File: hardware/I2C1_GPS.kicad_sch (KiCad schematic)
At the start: 0 parts

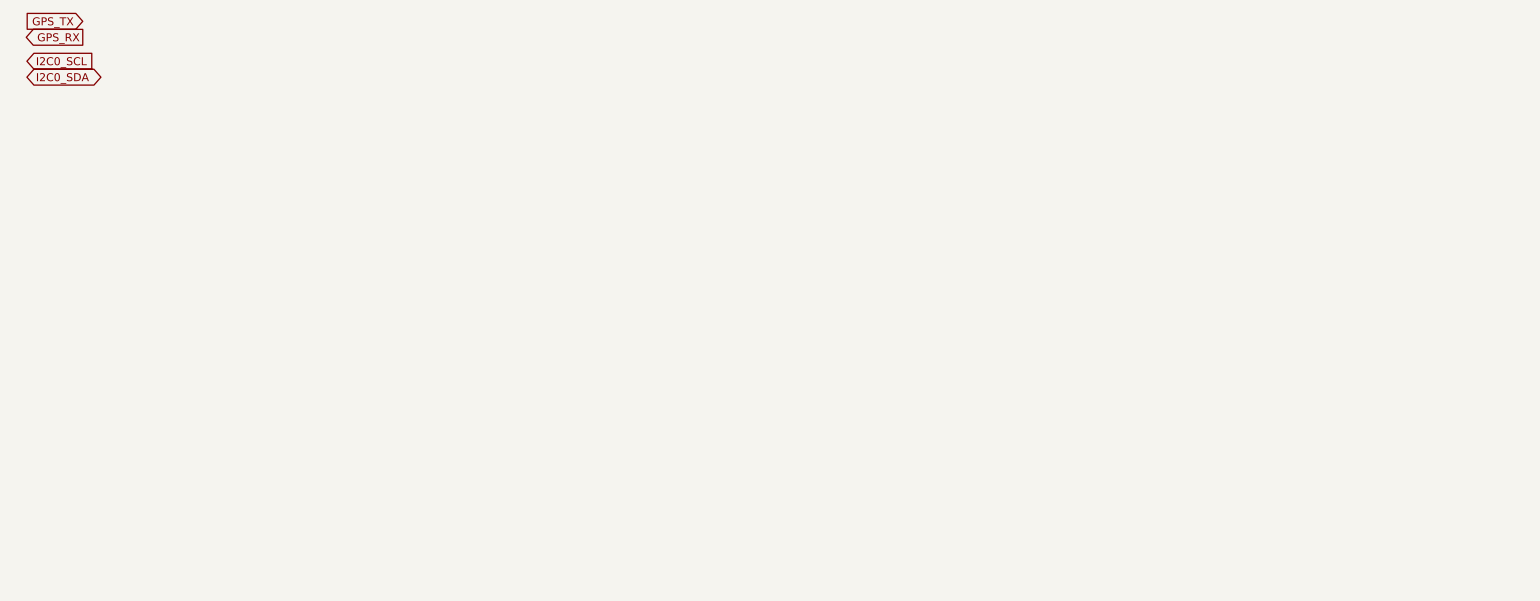
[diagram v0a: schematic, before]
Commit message: More work on the scehmatic for I2C0 and I2C1 + UART GPS.
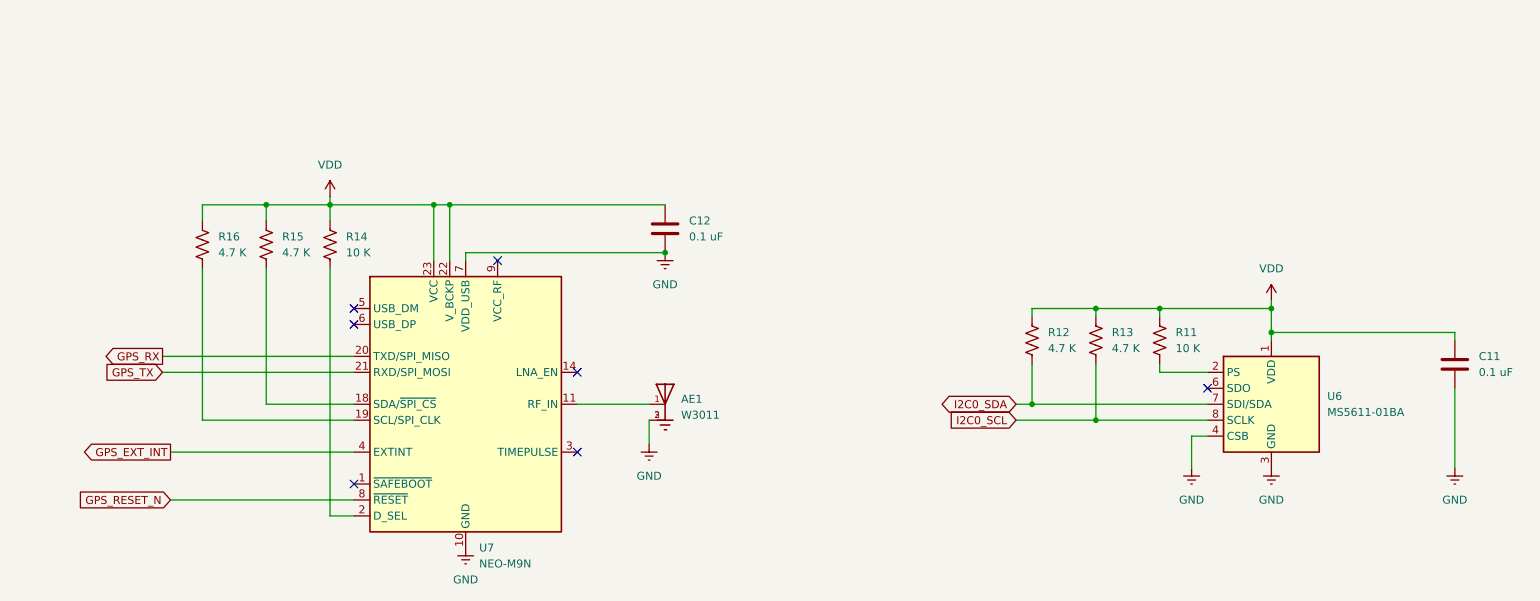
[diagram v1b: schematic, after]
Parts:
- added AE1: W3011, W3011:XDCR_W3011, symbol W3011:W3011
- added C11, C12: 0.1 uF, symbol Device:C
- added R11, R14: 10 K, symbol Device:R_US
- added R12, R13, R15, R16: 4.7 K, symbol Device:R_US
- added U6: MS5611-01BA, Package_LGA:LGA-8_3x5mm_P1.25mm, symbol Sensor_Pressure:MS5611-01BA
- added U7: NEO-M9N, RF_GPS:ublox_NEO, symbol RF_GPS:NEO-M9N
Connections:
- net GPS_RX: now also U7.20 (TXD/SPI_MISO)
- net GPS_TX: now also U7.21 (RXD/SPI_MOSI)
- net I2C0_SCL: now also R13.1, U6.8 (SCLK)
- net I2C0_SDA: now also R12.1, U6.7 (SDI/SDA)
- new net: R11.1, U6.2 (PS)
- new net: AE1.1, U7.11 (RF_IN)
- new net: R15.2, U7.18 (SDA/~{SPI_CS})
- new net: R16.2, U7.19 (SCL/SPI_CLK)
- new net: R14.2, U7.2 (D_SEL)
- new net GND: AE1.2, AE1.3, C11.2, C12.2, U6.3 (GND), U6.4 (CSB), U6.5 (CSB), U7.10 (GND), U7.12 (GND), U7.13 (GND), U7.24 (GND), U7.7 (VDD_USB)
- new net GPS_EXT_INT: U7.4 (EXTINT)
- new net GPS_RESET_N: U7.8 (~{RESET})
- new net VDD: C11.1, C12.1, R11.2, R12.2, R13.2, R14.1, R15.1, R16.1, U6.1 (VDD), U7.22 (V_BCKP), U7.23 (VCC)
- no-connect marks 0 -> 7

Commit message: Fixed EEC errors.
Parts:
- AE1: footprint W3011:XDCR_W3011 -> footprints:XDCR_W3011
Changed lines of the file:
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@@
 			)
 		)
-		(property "Footprint" "W3011:XDCR_W3011"
+		(property "Footprint" "footprints:XDCR_W3011"
 			(at 119.38 80.01 0)
 			(hide yes)

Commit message: Added footprints for the resitors.
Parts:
- R11, R12, R13, R14, R15, R16: footprint (none) -> Resistor_SMD:R_1206_3216Metric
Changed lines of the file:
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@@
 			)
 		)
-		(property "Footprint" ""
+		(property "Footprint" "Resistor_SMD:R_1206_3216Metric"
 			(at 197.104 69.596 90)
 			(hide yes)
@@
 			)
 		)
-		(property "Footprint" ""
+		(property "Footprint" "Resistor_SMD:R_1206_3216Metric"
 			(at 186.944 69.596 90)
 			(hide yes)
@@
 			)
 		)
-		(property "Footprint" ""
+		(property "Footprint" "Resistor_SMD:R_1206_3216Metric"
 			(at 67.056 54.864 90)
 			(hide yes)
@@
 			)
 		)
-		(property "Footprint" ""
+		(property "Footprint" "Resistor_SMD:R_1206_3216Metric"
 			(at 176.784 69.596 90)
 			(hide yes)
@@
 			)
 		)
-		(property "Footprint" ""
+		(property "Footprint" "Resistor_SMD:R_1206_3216Metric"
 			(at 56.896 54.864 90)
 			(hide yes)
@@
 			)
 		)
-		(property "Footprint" ""
+		(property "Footprint" "Resistor_SMD:R_1206_3216Metric"
 			(at 46.736 54.864 90)
 			(hide yes)

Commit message: Added capacitor footprints.
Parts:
- C11, C12: footprint (none) -> Capacitor_SMD:C_1206_3216Metric
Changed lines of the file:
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@@
 			)
 		)
-		(property "Footprint" ""
+		(property "Footprint" "Capacitor_SMD:C_1206_3216Metric"
 			(at 246.0752 77.47 0)
 			(hide yes)
@@
 			)
 		)
-		(property "Footprint" ""
+		(property "Footprint" "Capacitor_SMD:C_1206_3216Metric"
 			(at 120.3452 55.88 0)
 			(hide yes)

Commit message: Worked on footprints and hardware definations.
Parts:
- C11, C12: footprint Capacitor_SMD:C_1206_3216Metric -> Capacitor_SMD:C_0805_2012Metric; Digikey Link (none) -> https://www.digikey.com/en/products/detail/kyocera-avx/KGM2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; Digikey Part Number (none) -> 478-KGM21NR71H104KTCT-ND
- R11, R14: value 10 K -> 10k
- R12, R13, R15, R16: value 4.7 K -> 4.7k
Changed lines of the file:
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@@
 			)
 		)
-		(property "Value" "10 K"
+		(property "Value" "10k"
 			(at 200.66 71.1199 0)
 			(show_name no)
@@
 			)
 		)
-		(property "Value" "4.7 K"
+		(property "Value" "4.7k"
 			(at 190.5 71.1199 0)
 			(show_name no)
@@
 			)
 		)
-		(property "Value" "10 K"
+		(property "Value" "10k"
 			(at 68.58 55.8799 0)
 			(show_name no)
@@
 			)
 		)
-		(property "Value" "4.7 K"
+		(property "Value" "4.7k"
 			(at 180.34 71.1199 0)
 			(show_name no)
@@
 			)
 		)
-		(property "Value" "4.7 K"
+		(property "Value" "4.7k"
 			(at 58.42 55.8799 0)
 			(show_name no)
@@
 			)
 		)
-		(property "Footprint" "Capacitor_SMD:C_1206_3216Metric"
+		(property "Footprint" "Capacitor_SMD:C_0805_2012Metric"
 			(at 246.0752 77.47 0)
 			(hide yes)
@@
 			)
 		)
+		(property "Digikey Link" "https://www.digikey.com/en/products/detail/kyocera-avx/KGM21NR71H104KT/563505"
+			(at 245.11 73.66 0)
+			(hide yes)
+			(show_name no)
+			(do_not_autoplace no)
+			(effects
+				(font
+					(size 1.27 1.27)
+				)
+			)
+		)
+		(property "Digikey Part Number" "478-KGM21NR71H104KTCT-ND"
+			(at 245.11 73.66 0)
+			(hide yes)
+			(show_name no)
+			(do_not_autoplace no)
+			(effects
+				(font
+					(size 1.27 1.27)
+				)
+			)
+		)
 		(pin "1"
 		)
@@
 			)
 		)
-		(property "Footprint" "Capacitor_SMD:C_1206_3216Metric"
+		(property "Footprint" "Capacitor_SMD:C_0805_2012Metric"
 			(at 120.3452 55.88 0)
 			(hide yes)
@@
 			)
 		)
+		(property "Digikey Link" "https://www.digikey.com/en/products/detail/kyocera-avx/KGM21NR71H104KT/563505"
+			(at 119.38 52.07 0)
+			(hide yes)
+			(show_name no)
+			(do_not_autoplace no)
+			(effects
+				(font
+					(size 1.27 1.27)
+				)
+			)
+		)
+		(property "Digikey Part Number" "478-KGM21NR71H104KTCT-ND"
+			(at 119.38 52.07 0)
+			(hide yes)
+			(show_name no)
+			(do_not_autoplace no)
+			(effects
+				(font
+					(size 1.27 1.27)
+				)
+			)
+		)
 		(pin "1"
 		)
@@
 			)
 		)
-		(property "Value" "4.7 K"
+		(property "Value" "4.7k"
 			(at 48.26 55.8799 0)
 			(show_name no)

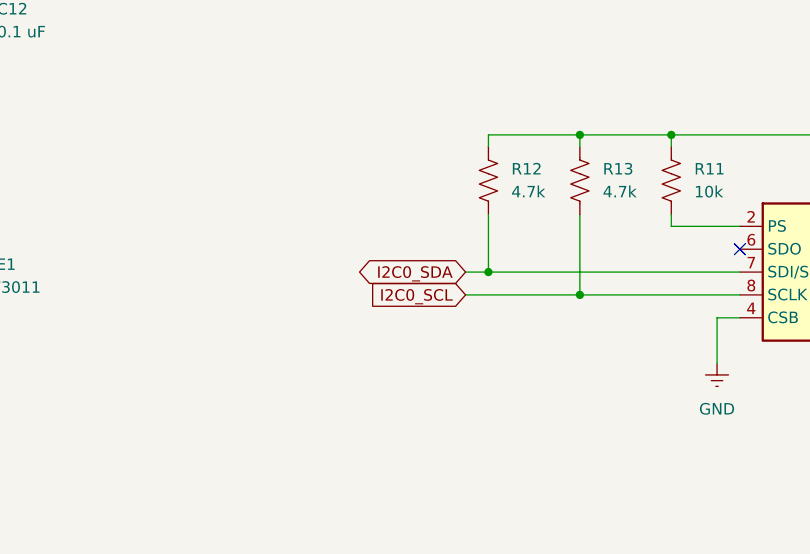
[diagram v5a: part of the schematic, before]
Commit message: Fixed I2C1 global labels.
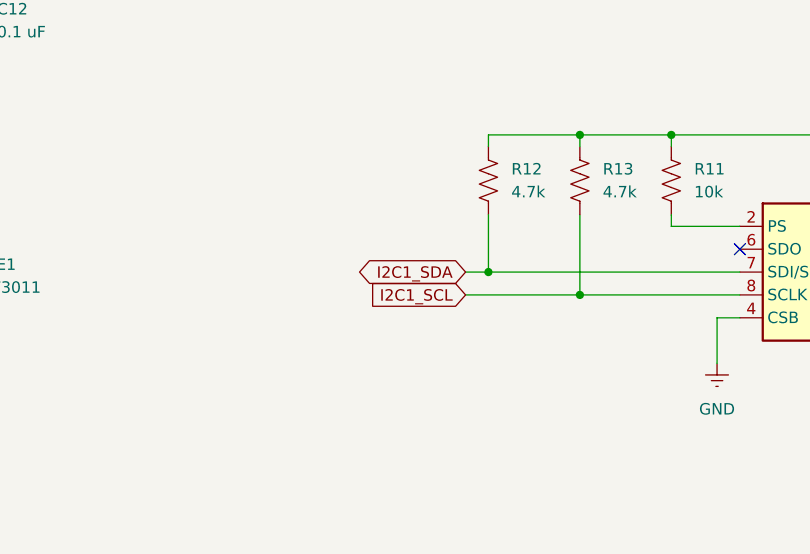
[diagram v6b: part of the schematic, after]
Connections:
- net I2C0_SCL renamed I2C1_SCL
- net I2C0_SDA renamed I2C1_SDA
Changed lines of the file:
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@@
 		)
 	)
-	(global_label "I2C0_SCL"
+	(global_label "I2C1_SCL"
 		(shape input)
 		(at 175.26 82.55 180)
@@
 		)
 	)
-	(global_label "I2C0_SDA"
+	(global_label "I2C1_SDA"
 		(shape bidirectional)
 		(at 175.26 80.01 180)

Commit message: Worked on PCB routing and component placement.
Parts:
- AE1: Digikey Link (none) -> https://www.digikey.com/en/products/detail/pulse-electronic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; Digikey Part Number (none) -> 553-2582-1-ND
- R11, R14: footprint Resistor_SMD:R_1206_3216Metric -> Resistor_SMD:R_0603_1608Metric; Digikey Link (none) -> https://www.digikey.com/en/products/detail/vishay/MCT06030C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; Digikey Part Number (none) -> MCT0603-10.0K-CFCT-ND
- R12, R13, R15, R16: footprint Resistor_SMD:R_1206_3216Metric -> Resistor_SMD:R_0603_1608Metric; Digikey Link (none) -> https://www.digikey.com/en/products/detail/vishay/MCT06030C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; Digikey Part Number (none) -> MCT0603-4.70K-CFCT-ND
- U6: Digikey Link (none) -> https://www.digikey.com/en/products/detail/te-connectivity-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; Digikey Part Number (none) -> 223-1622-1-ND
- U7: Digikey Link (none) -> https://www.digikey.com/en/products/detail/u-blox/NEO-M9N-0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; Digikey Part Number (none) -> 672-NEO-M9N-00BCT-ND
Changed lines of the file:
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@@
 			)
 		)
-		(property "Footprint" "Resistor_SMD:R_1206_3216Metric"
+		(property "Footprint" "Resistor_SMD:R_0603_1608Metric"
 			(at 197.104 69.596 90)
 			(hide yes)
@@
 		)
 		(property "Description" "Resistor, US symbol"
+			(at 198.12 69.85 0)
+			(hide yes)
+			(show_name no)
+			(do_not_autoplace no)
+			(effects
+				(font
+					(size 1.27 1.27)
+				)
+			)
+		)
+		(property "Digikey Link" "https://www.digikey.com/en/products/detail/vishay/MCT06030C1002FP500/1850440"
+			(at 198.12 69.85 0)
+			(hide yes)
+			(show_name no)
+			(do_not_autoplace no)
+			(effects
+				(font
+					(size 1.27 1.27)
+				)
+			)
+		)
+		(property "Digikey Part Number" "MCT0603-10.0K-CFCT-ND"
 			(at 198.12 69.85 0)
 			(hide yes)
@@
 			)
 		)
+		(property "Digikey Link" "https://www.digikey.com/en/products/detail/pulse-electronics/W3011/3025804"
+			(at 119.38 80.01 0)
+			(hide yes)
+			(show_name no)
+			(do_not_autoplace no)
+			(effects
+				(font
+					(size 1.27 1.27)
+				)
+			)
+		)
+		(property "Digikey Part Number" "553-2582-1-ND"
+			(at 119.38 80.01 0)
+			(hide yes)
+			(show_name no)
+			(do_not_autoplace no)
+			(effects
+				(font
+					(size 1.27 1.27)
+				)
+			)
+		)
 		(pin "3"
 		)
@@
 			)
 		)
+		(property "Digikey Link" "https://www.digikey.com/en/products/detail/te-connectivity-measurement-specialties/MS561101BA03-50/5277445"
+			(at 215.9 80.01 0)
+			(hide yes)
+			(show_name no)
+			(do_not_autoplace no)
+			(effects
+				(font
+					(size 1.27 1.27)
+				)
+			)
+		)
+		(property "Digikey Part Number" "223-1622-1-ND"
+			(at 215.9 80.01 0)
+			(hide yes)
+			(show_name no)
+			(do_not_autoplace no)
+			(effects
+				(font
+					(size 1.27 1.27)
+				)
+			)
+		)
 		(pin "5"
 		)
@@
 			)
 		)
-		(property "Footprint" "Resistor_SMD:R_1206_3216Metric"
+		(property "Footprint" "Resistor_SMD:R_0603_1608Metric"
 			(at 186.944 69.596 90)
 			(hide yes)
@@
 		)
 		(property "Description" "Resistor, US symbol"
+			(at 187.96 69.85 0)
+			(hide yes)
+			(show_name no)
+			(do_not_autoplace no)
+			(effects
+				(font
+					(size 1.27 1.27)
+				)
+			)
+		)
+		(property "Digikey Link" "https://www.digikey.com/en/products/detail/vishay/MCT06030C4701FP500/2607853"
+			(at 187.96 69.85 0)
+			(hide yes)
+			(show_name no)
+			(do_not_autoplace no)
+			(effects
+				(font
+					(size 1.27 1.27)
+				)
+			)
+		)
+		(property "Digikey Part Number" "MCT0603-4.70K-CFCT-ND"
 			(at 187.96 69.85 0)
 			(hide yes)
@@
 			)
 		)
+		(property "Digikey Link" "https://www.digikey.com/en/products/detail/u-blox/NEO-M9N-00B/12149174?s=N4IgTCBcDaIHYFMD2BaAtgTjiAugXyA"
+			(at 87.63 80.01 0)
+			(hide yes)
+			(show_name no)
+			(do_not_autoplace no)
+			(effects
+				(font
+					(size 1.27 1.27)
+				)
+			)
+		)
+		(property "Digikey Part Number" "672-NEO-M9N-00BCT-ND"
+			(at 87.63 80.01 0)
+			(hide yes)
+			(show_name no)
+			(do_not_autoplace no)
+			(effects
+				(font
+					(size 1.27 1.27)
+				)
+			)
+		)
 		(pin "13"
 		)
@@
 			)
 		)
-		(property "Footprint" "Resistor_SMD:R_1206_3216Metric"
+		(property "Footprint" "Resistor_SMD:R_0603_1608Metric"
 			(at 67.056 54.864 90)
 			(hide yes)
@@
 		)
 		(property "Description" "Resistor, US symbol"
+			(at 66.04 54.61 0)
+			(hide yes)
+			(show_name no)
+			(do_not_autoplace no)
+			(effects
+				(font
+					(size 1.27 1.27)
+				)
+			)
+		)
+		(property "Digikey Link" "https://www.digikey.com/en/products/detail/vishay/MCT06030C1002FP500/1850440"
+			(at 66.04 54.61 0)
+			(hide yes)
+			(show_name no)
+			(do_not_autoplace no)
+			(effects
+				(font
+					(size 1.27 1.27)
+				)
+			)
+		)
+		(property "Digikey Part Number" "MCT0603-10.0K-CFCT-ND"
 			(at 66.04 54.61 0)
 			(hide yes)
@@
 			)
 		)
-		(property "Footprint" "Resistor_SMD:R_1206_3216Metric"
+		(property "Footprint" "Resistor_SMD:R_0603_1608Metric"
 			(at 176.784 69.596 90)
 			(hide yes)
@@
 		)
 		(property "Description" "Resistor, US symbol"
+			(at 177.8 69.85 0)
+			(hide yes)
+			(show_name no)
+			(do_not_autoplace no)
+			(effects
+				(font
+					(size 1.27 1.27)
+				)
+			)
+		)
+		(property "Digikey Link" "https://www.digikey.com/en/products/detail/vishay/MCT06030C4701FP500/2607853"
+			(at 177.8 69.85 0)
+			(hide yes)
+			(show_name no)
+			(do_not_autoplace no)
+			(effects
+				(font
+					(size 1.27 1.27)
+				)
+			)
+		)
+		(property "Digikey Part Number" "MCT0603-4.70K-CFCT-ND"
 			(at 177.8 69.85 0)
 			(hide yes)
@@
 			)
 		)
-		(property "Footprint" "Resistor_SMD:R_1206_3216Metric"
+		(property "Footprint" "Resistor_SMD:R_0603_1608Metric"
 			(at 56.896 54.864 90)
 			(hide yes)
@@
 		)
 		(property "Description" "Resistor, US symbol"
+			(at 55.88 54.61 0)
+			(hide yes)
+			(show_name no)
+			(do_not_autoplace no)
+			(effects
+				(font
+					(size 1.27 1.27)
+				)
+			)
+		)
+		(property "Digikey Link" "https://www.digikey.com/en/products/detail/vishay/MCT06030C4701FP500/2607853"
+			(at 55.88 54.61 0)
+			(hide yes)
+			(show_name no)
+			(do_not_autoplace no)
+			(effects
+				(font
+					(size 1.27 1.27)
+				)
+			)
+		)
+		(property "Digikey Part Number" "MCT0603-4.70K-CFCT-ND"
 			(at 55.88 54.61 0)
 			(hide yes)
@@
 			)
 		)
-		(property "Footprint" "Resistor_SMD:R_1206_3216Metric"
+		(property "Footprint" "Resistor_SMD:R_0603_1608Metric"
 			(at 46.736 54.864 90)
 			(hide yes)
@@
 			(at 45.72 54.61 0)
 			(hide yes)
+			(show_name no)
+			(do_not_autoplace no)
+			(effects
+				(font
+					(size 1.27 1.27)
+				)
+			)
+		)
+		(property "Digikey Link" "https://www.digikey.com/en/products/detail/vishay/MCT06030C4701FP500/2607853"
+			(at 45.72 54.61 0)
+			(hide yes)
+			(show_name no)
+			(do_not_autoplace no)
+			(effects
+				(font
+					(size 1.27 1.27)
+				)
+			)
+		)
+		(property "Digikey Part Number" "MCT0603-4.70K-CFCT-ND"
+			(at 45.72 54.61 0)
+			(hide yes)
